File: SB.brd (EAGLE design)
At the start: 68 x 30 mm, 34 parts, among them IC1 ATMEGA32U4NT-TQFP, J1 USB-6P-SMT, J2 RJ12, J3 AUDIO-JACK-PJ321, J4 NO/NC, K1 HE721C-DIP, Q1 2N7002, Q2 2N7002

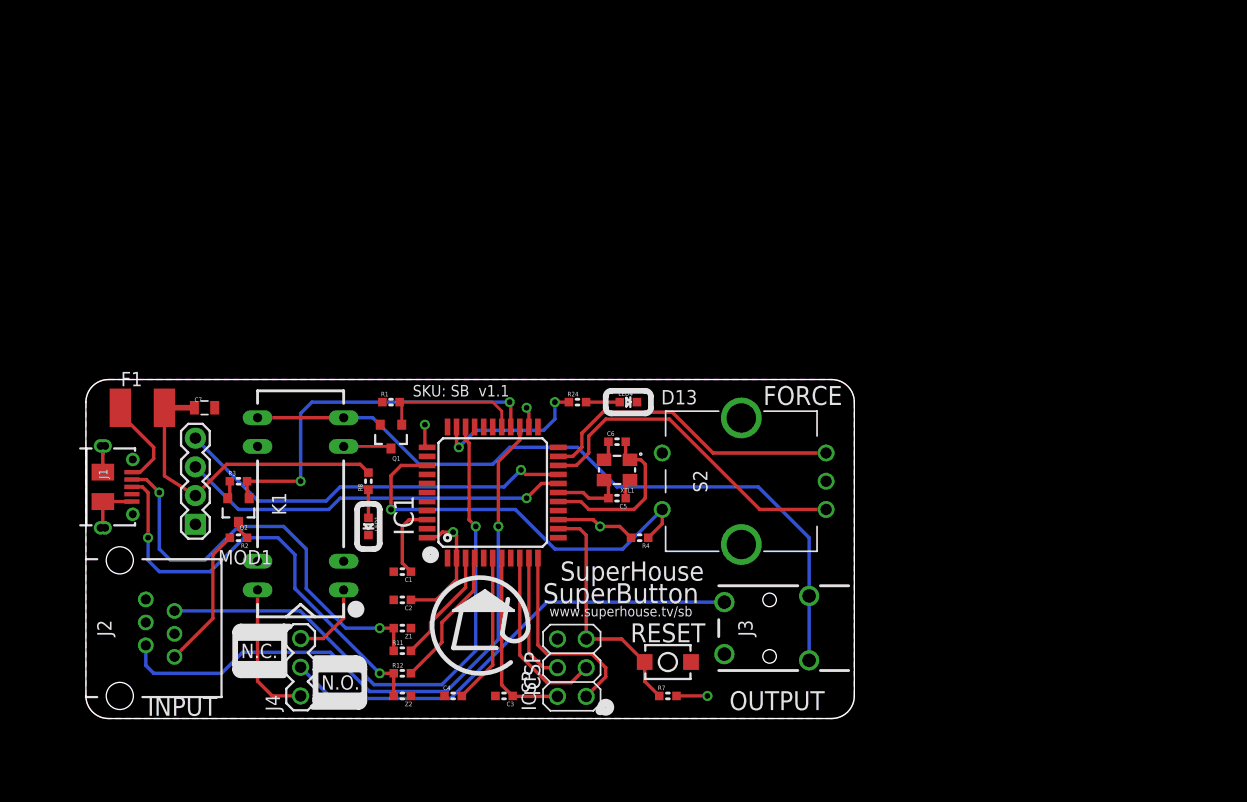
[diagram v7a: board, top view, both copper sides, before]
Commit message: Added HX711 strain gauge amplifier directly on controller instead of external
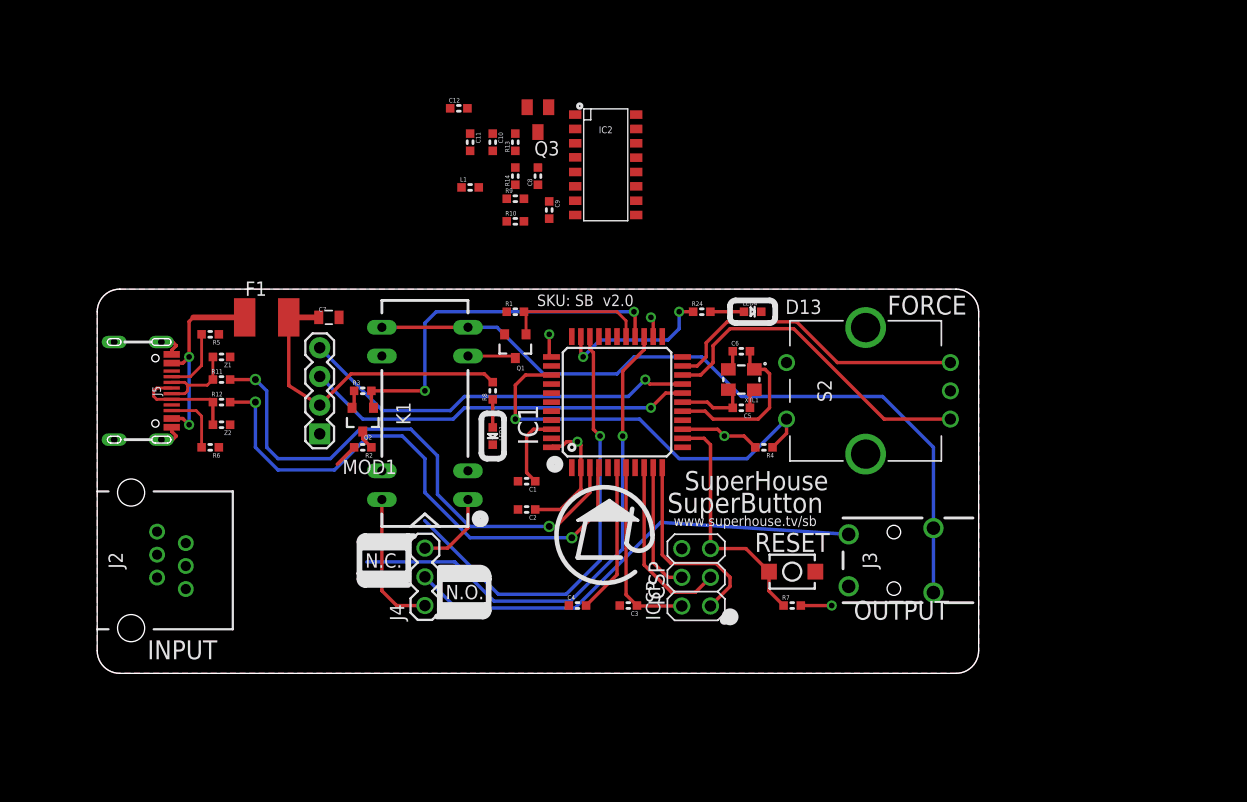
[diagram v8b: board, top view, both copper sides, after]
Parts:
- removed J1: USB-6P-SMT, SuperHouse-Connectors:USB-MICROB-MB05PMXX
- added C10, C12: 10uF, SuperHouse-DiscreteSemi:C0603
- added C11, C8, C9: 100nF, SuperHouse-DiscreteSemi:C0603
- added IC2: HX711-SOP16L, SuperHouse-ICs:SOP16-L
- added J5: USB-C-16P-16P, SuperHouse-Connectors:USB-C-16P
- added L1: 3.3uH, SuperHouse-DiscreteSemi:0603
- added Q3: 2N3906, SuperHouse-DiscreteSemi:SOT23-BEC
- added R10, R9: 100R, SuperHouse-DiscreteSemi:R0603
- added R13: 10K, SuperHouse-DiscreteSemi:R0603
- added R14: 8K2, SuperHouse-DiscreteSemi:R0603
- added R5, R6: 4K7, SuperHouse-DiscreteSemi:R0603
- MOD1: value OLED-I2C128X32-0.91-HEADER -> OLED-I2C-128X32-0.91; device SuperHouse-Displays:OLED-128X32-0.91-HEADER -> SuperHouse-Displays:OLED-128X32-0.91
- moved R11 28.8 mm to (12.0, 31.0)
- moved R12 28.8 mm to (12.0, 29.0)
- moved Z1 28.8 mm to (12.0, 33.0)
- moved Z2 28.8 mm to (12.0, 27.0)
- moved C1 13.6 mm to (39.0, 22.0)
- moved C2 13.6 mm to (39.0, 19.5)
- moved C3 13.6 mm to (48.0, 11.0)
- moved C4 13.6 mm to (43.5, 11.0)
- moved C5 13.6 mm to (58.0, 28.5)
- moved C6 13.6 mm to (58.0, 33.5)
- moved C7 13.6 mm to (21.5, 36.5)
- moved F1 13.6 mm to (16.0, 36.5)
- moved IC1 13.6 mm to (47.0, 29.0)
- moved ICSP 13.6 mm to (54.0, 13.5)
- moved J4 13.6 mm to (30.0, 11.0)
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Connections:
- new net A+: J2.4, R10.1
- new net A-: J2.3, R9.1
- new net E+: C10.1, C11.1, J2.1, L1.1
- new net N$10: J5.B5, R6.2
- new net N$13: J5.A5, R5.2
- new net N$14: C9.1, IC2.7, R9.2
- new net N$15: C9.2, IC2.8, R10.2
- new net N$16: IC2.3, L1.2, Q3.C, R13.2
- new net N$17: C8.1, IC2.6
- new net N$20: IC2.2, Q3.B
- new net N$21: IC2.4, R13.1, R14.2
- new net XO: IC2.13
- net 5V: now also C12.1, IC2.1, IC2.16, J2.6, Q3.E; no longer J2.3, J2.4
- net D+: now also J5.A6, J5.B6; no longer J1.D+
- net D-: now also J5.A7, J5.B7; no longer J1.D-
- net D4_A6: now also IC2.11; no longer J2.5
- net D5: now also IC2.12; no longer J2.2
- net GND: now also C10.2, C11.2, C12.2, C8.2, IC2.14, IC2.15, IC2.5, J2.2, J5.A12B1, J5.A1B12, J5.FIX1, J5.FIX2, J5.FIX3, J5.FIX4, R14.1, R5.1, R6.1; no longer J1.FIX1, J1.FIX2, J1.GND, J1.TAB1, J1.TAB2, J2.1
- net N$2: now also J2.5; no longer J2.6
- net USB+: now also J5.A4B9, J5.A9B4; no longer J1.VBUS
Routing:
- net RD-: track 10.2 -> 47.8 mm, vias 0 -> 2
- net RD+: track 12.5 -> 49.0 mm, vias 0 -> 2
- net D-: track 38.1 -> 7.96 mm, vias 2 -> 0
- net D+: track 39.8 -> 9.64 mm, vias 2 -> 0
- net D4_A6: track 57.0 -> 45.6 mm
- net D5: track 50.8 -> 39.6 mm
- net N$2: track 12.6 -> 2.12 mm
- net USB+: track 8.14 -> 17.7 mm, vias 0 -> 2
- net N$13: track 0.00 -> 5.81 mm
- net N$10: track 0.00 -> 5.61 mm
- net GND: track 13.2 -> 10.1 mm
- net N$7: track 65.3 -> 67.3 mm
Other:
- board size 68 x 30 mm -> 78 x 34 mm
- board text added: "SKU: SB v2.0"
- board text removed: "SKU: SB v1.1"
